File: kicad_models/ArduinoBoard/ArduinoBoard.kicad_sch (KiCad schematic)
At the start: 7 parts, among them J1 5V Output, J2 Buttons, J3 PWM Output, J4 Screw_Terminal_01x02, J5 Conn_01x04_Pin, J6 OLED

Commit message: Updated the KiCad files.
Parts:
- removed J6: OLED, symbol Connector:Screw_Terminal_01x04
- added J6: OLED, Connector_PinHeader_2.54mm:PinHeader_1x04_P2.54mm_Vertical, symbol Connector:Conn_01x04_Pin
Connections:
- net at A1.23 (A4): now also J6.4 (Pin_4)
- net at A1.24 (A5): now also J6.3 (Pin_3)
- net at A1.27 (+5V), J1.2 (Pin_2): now also J6.2 (Pin_2)
- net at A1.4 (GND), J1.1 (Pin_1): now also J6.1 (Pin_1)
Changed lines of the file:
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@@
 	)
 	(junction
-		(at 137.16 59.69)
+		(at 129.54 130.81)
 		(diameter 0)
 		(color 0 0 0 0)
 	)
+	(junction
+		(at 115.57 57.15)
+		(diameter 0)
+		(color 0 0 0 0)
+	)
 	(wire
 		(pts
@@
 	(wire
 		(pts
+			(xy 152.4 135.89) (xy 152.4 104.14)
+		)
+		(stroke
+			(width 0)
+			(type default)
+		)
+	)
+	(wire
+		(pts
 			(xy 134.62 130.81) (xy 134.62 119.38)
 		)
@@
 	(wire
 		(pts
+			(xy 129.54 130.81) (xy 129.54 135.89)
+		)
+		(stroke
+			(width 0)
+			(type default)
+		)
+	)
+	(wire
+		(pts
 			(xy 134.62 130.81) (xy 165.1 130.81)
 		)
@@
 	(wire
 		(pts
+			(xy 130.81 135.89) (xy 132.08 135.89)
+		)
+		(stroke
+			(width 0)
+			(type default)
+		)
+	)
+	(wire
+		(pts
+			(xy 134.62 133.35) (xy 149.86 133.35)
+		)
+		(stroke
+			(width 0)
+			(type default)
+		)
+	)
+	(wire
+		(pts
 			(xy 168.91 104.14) (xy 168.91 118.11)
 		)
@@
 	(wire
 		(pts
-			(xy 137.16 59.69) (xy 154.94 59.69)
+			(xy 137.16 135.89) (xy 152.4 135.89)
 		)
 		(stroke
@@
 	(wire
 		(pts
-			(xy 96.52 57.15) (xy 137.16 57.15)
+			(xy 96.52 57.15) (xy 115.57 57.15)
 		)
 		(stroke
@@
 	(wire
 		(pts
-			(xy 96.52 130.81) (xy 132.08 130.81)
+			(xy 96.52 130.81) (xy 129.54 130.81)
 		)
 		(stroke
@@
 	(wire
 		(pts
-			(xy 137.16 59.69) (xy 137.16 68.58)
+			(xy 144.78 104.14) (xy 152.4 104.14)
 		)
 		(stroke
@@
 	(wire
 		(pts
+			(xy 149.86 106.68) (xy 144.78 106.68)
+		)
+		(stroke
+			(width 0)
+			(type default)
+		)
+	)
+	(wire
+		(pts
 			(xy 170.18 120.65) (xy 165.1 120.65)
 		)
@@
 	(wire
 		(pts
+			(xy 129.54 130.81) (xy 132.08 130.81)
+		)
+		(stroke
+			(width 0)
+			(type default)
+		)
+	)
+	(wire
+		(pts
 			(xy 187.96 104.14) (xy 187.96 80.01)
 		)
@@
 	(wire
 		(pts
+			(xy 134.62 135.89) (xy 134.62 133.35)
+		)
+		(stroke
+			(width 0)
+			(type default)
+		)
+	)
+	(wire
+		(pts
 			(xy 184.15 100.33) (xy 184.15 82.55)
 		)
@@
 	(wire
 		(pts
+			(xy 130.81 125.73) (xy 130.81 135.89)
+		)
+		(stroke
+			(width 0)
+			(type default)
+		)
+	)
+	(wire
+		(pts
+			(xy 115.57 57.15) (xy 137.16 57.15)
+		)
+		(stroke
+			(width 0)
+			(type default)
+		)
+	)
+	(wire
+		(pts
+			(xy 115.57 125.73) (xy 130.81 125.73)
+		)
+		(stroke
+			(width 0)
+			(type default)
+		)
+	)
+	(wire
+		(pts
+			(xy 115.57 125.73) (xy 115.57 57.15)
+		)
+		(stroke
+			(width 0)
+			(type default)
+		)
+	)
+	(wire
+		(pts
 			(xy 96.52 72.39) (xy 96.52 130.81)
 		)
@@
 	(wire
 		(pts
-			(xy 137.16 57.15) (xy 137.16 59.69)
-		)
-		(stroke
-			(width 0)
-			(type default)
-		)
-	)
-	(wire
-		(pts
-			(xy 154.94 138.43) (xy 154.94 59.69)
+			(xy 137.16 57.15) (xy 137.16 68.58)
 		)
 		(stroke
@@
 		(pts
 			(xy 180.34 85.09) (xy 176.53 85.09)
+		)
+		(stroke
+			(width 0)
+			(type default)
+		)
+	)
+	(wire
+		(pts
+			(xy 149.86 133.35) (xy 149.86 106.68)
 		)
 		(stroke
@@
 	)
 	(symbol
-		(lib_id "Connector:Screw_Terminal_01x04")
-		(at 135.89 143.51 270)
+		(lib_id "Connector:Conn_01x04_Pin")
+		(at 132.08 140.97 90)
 		(unit 1)
 		(exclude_from_sim no)
@@
 		(fields_autoplaced yes)
 		(property "Reference" "J6"
-			(at 134.62 147.32 90)
+			(at 133.35 143.51 90)
 			(effects
 				(font
@@
 		)
 		(property "Value" "OLED"
-			(at 134.62 149.86 90)
-			(effects
-				(font
-					(size 1.27 1.27)
-				)
-			)
-		)
-		(property "Footprint" ""
-			(at 135.89 143.51 0)
+			(at 133.35 146.05 90)
+			(effects
+				(font
+					(size 1.27 1.27)
+				)
+			)
+		)
+		(property "Footprint" "Connector_PinHeader_2.54mm:PinHeader_1x04_P2.54mm_Vertical"
+			(at 132.08 140.97 0)
 			(effects
 				(font
@@
 		)
 		(property "Datasheet" "~"
-			(at 135.89 143.51 0)
-			(effects
-				(font
-					(size 1.27 1.27)
-				)
-				(hide yes)
-			)
-		)
-		(property "Description" "Generic screw terminal, single row, 01x04, script generated (kicad-library-utils/schlib/autogen/connector/)"
-			(at 135.89 143.51 0)
+			(at 132.08 140.97 0)
+			(effects
+				(font
+					(size 1.27 1.27)
+				)
+				(hide yes)
+			)
+		)
+		(property "Description" "Generic connector, single row, 01x04, script generated"
+			(at 132.08 140.97 0)
 			(effects
 				(font
@@
 		(pin "2"
 		)
+		(pin "4"
+		)
+		(pin "3"
+		)
 		(pin "1"
 		)
-		(pin "3"
-		)
-		(pin "4"
-		)
 		(instances
-			(project ""
+			(project "ArduinoBoard"
 				(path "/98bf385f-4cd5-4c0c-bda4-6735edf00281"
 					(reference "J6")

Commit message: Updated the PCB file I was working on.
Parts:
- added H1, H2, H3, H4: MountingHole, MountingHole:MountingHole_2.2mm_M2_DIN965_Pad, symbol Mechanical:MountingHole

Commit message: Updated the kicad files some more
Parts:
- J1, J2, J3, J4: footprint TerminalBlock:TerminalBlock_MaiXu_MX126-5.0-02P_1x02_P5.00mm -> TerminalBlock:TerminalBlock_bornier-2_P5.08mm
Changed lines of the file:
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@@
 			)
 		)
-		(property "Footprint" "TerminalBlock:TerminalBlock_MaiXu_MX126-5.0-02P_1x02_P5.00mm"
+		(property "Footprint" "TerminalBlock:TerminalBlock_bornier-2_P5.08mm"
 			(at 175.26 118.11 0)
 			(effects
@@
 			)
 		)
-		(property "Footprint" "TerminalBlock:TerminalBlock_MaiXu_MX126-5.0-02P_1x02_P5.00mm"
+		(property "Footprint" "TerminalBlock:TerminalBlock_bornier-2_P5.08mm"
 			(at 80.01 106.68 0)
 			(effects
@@
 			)
 		)
-		(property "Footprint" "TerminalBlock:TerminalBlock_MaiXu_MX126-5.0-02P_1x02_P5.00mm"
+		(property "Footprint" "TerminalBlock:TerminalBlock_bornier-2_P5.08mm"
 			(at 80.01 88.9 0)
 			(effects
@@
 			)
 		)
-		(property "Footprint" "TerminalBlock:TerminalBlock_MaiXu_MX126-5.0-02P_1x02_P5.00mm"
+		(property "Footprint" "TerminalBlock:TerminalBlock_bornier-2_P5.08mm"
 			(at 80.01 72.39 0)
 			(effects

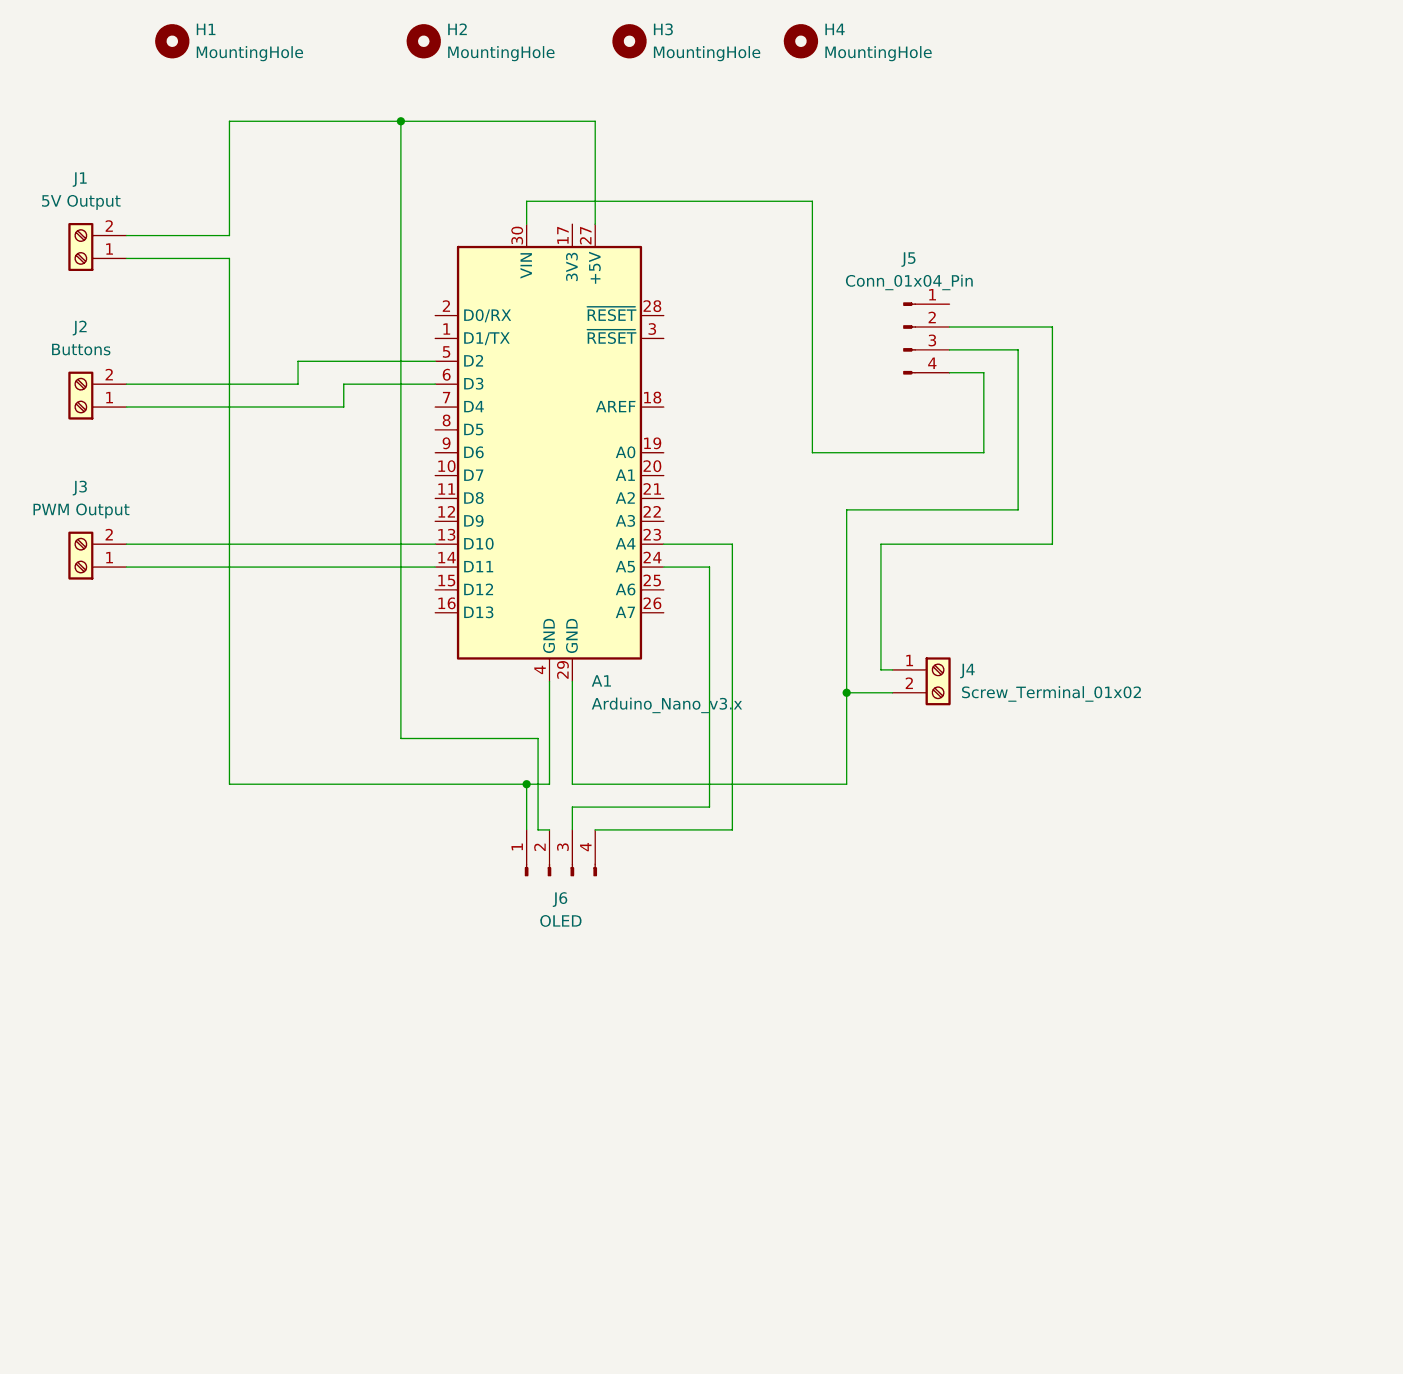
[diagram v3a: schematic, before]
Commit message: Had to make some updates after my first prototype PCB. Hopefully this version is correct. :)
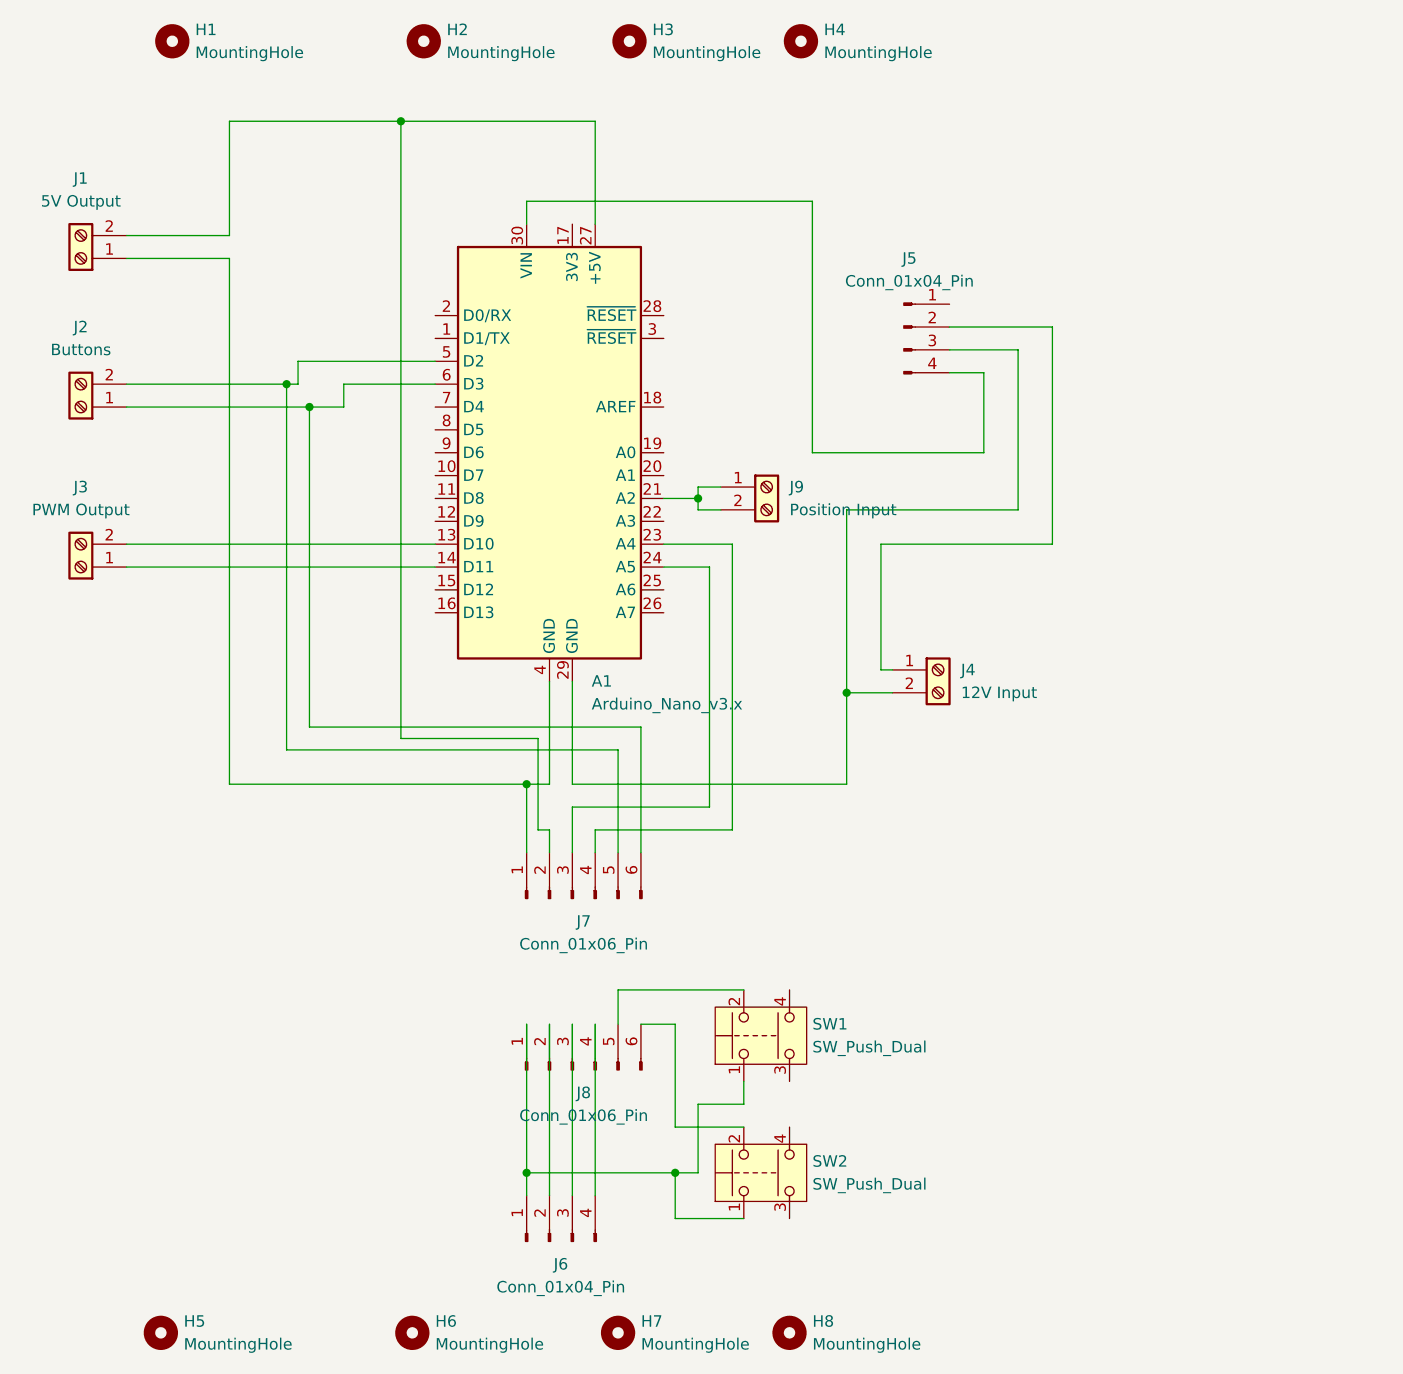
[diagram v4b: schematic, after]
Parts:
- added H5, H6, H7, H8: MountingHole, MountingHole:MountingHole_2.2mm_M2_DIN965_Pad, symbol Mechanical:MountingHole
- added J7, J8: Conn_01x06_Pin, Connector_PinHeader_2.54mm:PinHeader_1x06_P2.54mm_Vertical, symbol Connector:Conn_01x06_Pin
- added J9: Position Input, TerminalBlock:TerminalBlock_bornier-2_P5.08mm, symbol Connector:Screw_Terminal_01x02
- added SW1, SW2: SW_Push_Dual, Button_Switch_THT:SW_PUSH-12mm, symbol Switch:SW_Push_Dual
- J4: value Screw_Terminal_01x02 -> 12V Input
- J6: value OLED -> Conn_01x04_Pin
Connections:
- net at A1.21 (A2): now also J9.1 (Pin_1), J9.2 (Pin_2)
- net at A1.23 (A4): now also J7.4 (Pin_4); no longer J6.4 (Pin_4)
- net at A1.24 (A5): now also J7.3 (Pin_3); no longer J6.3 (Pin_3)
- net at A1.27 (+5V), J1.2 (Pin_2): now also J7.2 (Pin_2); no longer J6.2 (Pin_2)
- net at A1.4 (GND), J1.1 (Pin_1): now also J7.1 (Pin_1); no longer J6.1 (Pin_1)
- net at A1.5 (D2), J2.2 (Pin_2): now also J7.5 (Pin_5)
- net at A1.6 (D3), J2.1 (Pin_1): now also J7.6 (Pin_6)
- new net: J6.1 (Pin_1), J8.1 (Pin_1), SW1.1, SW2.1
- new net: J6.2 (Pin_2), J8.2 (Pin_2)
- new net: J6.3 (Pin_3), J8.3 (Pin_3)
- new net: J6.4 (Pin_4), J8.4 (Pin_4)
- new net: J8.6 (Pin_6), SW2.2
- new net: J8.5 (Pin_5), SW1.2

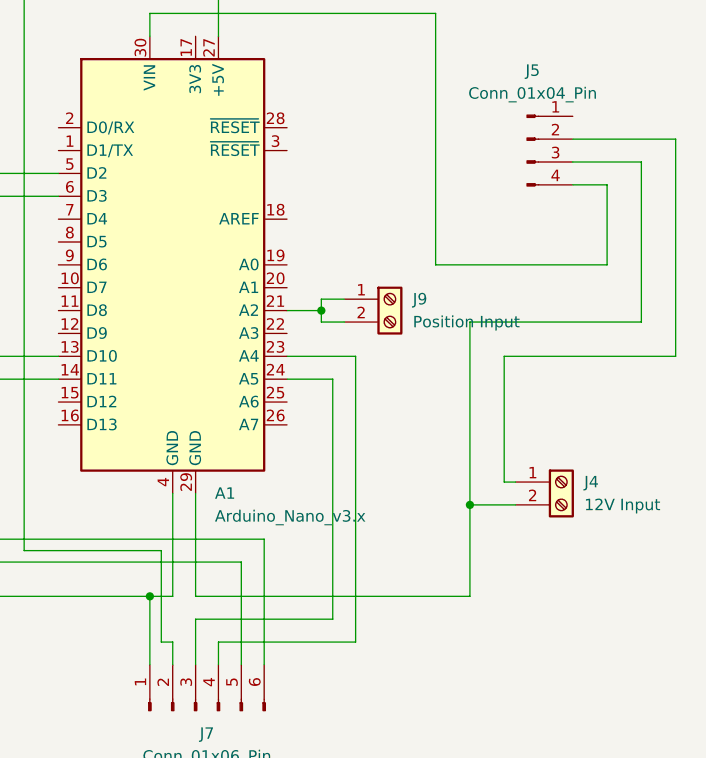
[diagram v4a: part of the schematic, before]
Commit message: Added a 0.1uF capacitor and linked the two GND pins on the Arduino. I seem to have overloaded the Arduino when I plugged in the 12V input - probably a surge. The capacitor should condition the circuit momentarily.
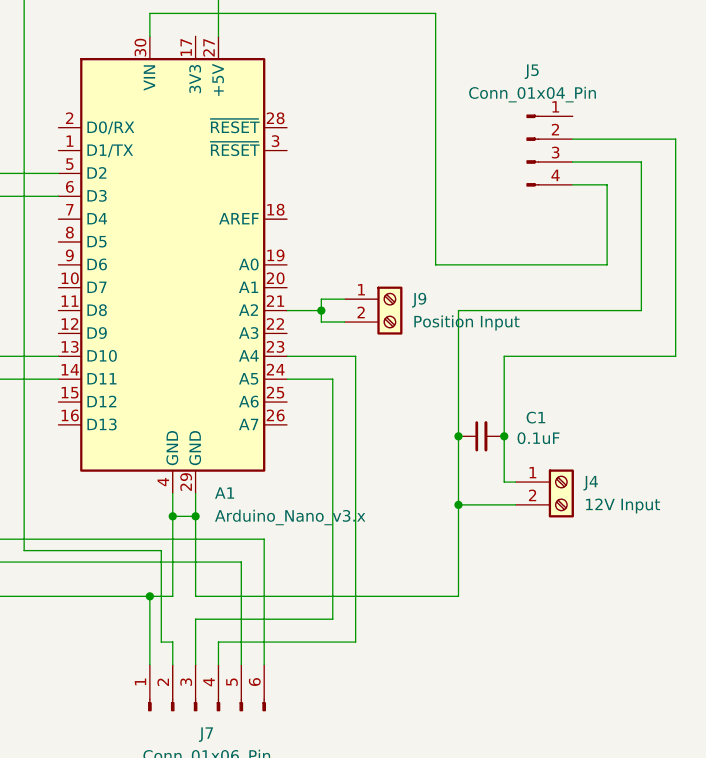
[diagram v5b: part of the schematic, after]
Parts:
- added C1: 0.1uF, Capacitor_THT:C_Disc_D3.0mm_W2.0mm_P2.50mm, symbol Device:C_Small
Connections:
- net at J4.1 (Pin_1), J5.2 (Pin_2): now also C1.2
- net at A1.29 (GND), J4.2 (Pin_2), J5.3 (Pin_3): now also A1.4 (GND), J1.1 (Pin_1), J7.1 (Pin_1), C1.1
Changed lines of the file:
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@@
 	(paper "A4")
 	(junction
-		(at 165.1 120.65)
+		(at 163.83 120.65)
 		(diameter 0)
 		(color 0 0 0 0)
@@
 	)
 	(junction
+		(at 134.62 121.92)
+		(diameter 0)
+		(color 0 0 0 0)
+	)
+	(junction
 		(at 115.57 57.15)
+		(diameter 0)
+		(color 0 0 0 0)
+	)
+	(junction
+		(at 163.83 113.03)
 		(diameter 0)
 		(color 0 0 0 0)
@@
 	)
 	(junction
+		(at 168.91 113.03)
+		(diameter 0)
+		(color 0 0 0 0)
+	)
+	(junction
+		(at 132.08 121.92)
+		(diameter 0)
+		(color 0 0 0 0)
+	)
+	(junction
 		(at 146.05 173.99)
 		(diameter 0)
@@
 	(wire
 		(pts
+			(xy 132.08 121.92) (xy 132.08 119.38)
+		)
+		(stroke
+			(width 0)
+			(type default)
+		)
+	)
+	(wire
+		(pts
 			(xy 180.34 93.98) (xy 180.34 85.09)
 		)
@@
 	(wire
 		(pts
-			(xy 134.62 130.81) (xy 134.62 119.38)
+			(xy 134.62 130.81) (xy 134.62 121.92)
 		)
 		(stroke
@@
 	(wire
 		(pts
-			(xy 165.1 100.33) (xy 184.15 100.33)
+			(xy 163.83 99.06) (xy 184.15 99.06)
 		)
 		(stroke
@@
 	(wire
 		(pts
-			(xy 132.08 130.81) (xy 132.08 119.38)
+			(xy 132.08 130.81) (xy 132.08 121.92)
 		)
 		(stroke
@@
 	(wire
 		(pts
-			(xy 134.62 130.81) (xy 165.1 130.81)
-		)
-		(stroke
-			(width 0)
-			(type default)
-		)
-	)
-	(wire
-		(pts
-			(xy 165.1 100.33) (xy 165.1 120.65)
+			(xy 134.62 130.81) (xy 163.83 130.81)
+		)
+		(stroke
+			(width 0)
+			(type default)
+		)
+	)
+	(wire
+		(pts
+			(xy 163.83 99.06) (xy 163.83 113.03)
 		)
 		(stroke
@@
 	(wire
 		(pts
-			(xy 168.91 104.14) (xy 168.91 118.11)
+			(xy 168.91 104.14) (xy 168.91 113.03)
 		)
 		(stroke
@@
 	(wire
 		(pts
-			(xy 165.1 120.65) (xy 165.1 130.81)
+			(xy 163.83 120.65) (xy 163.83 130.81)
 		)
 		(stroke
@@
 	(wire
 		(pts
-			(xy 170.18 120.65) (xy 165.1 120.65)
+			(xy 170.18 120.65) (xy 163.83 120.65)
 		)
 		(stroke
@@
 	(wire
 		(pts
+			(xy 168.91 113.03) (xy 168.91 118.11)
+		)
+		(stroke
+			(width 0)
+			(type default)
+		)
+	)
+	(wire
+		(pts
 			(xy 134.62 133.35) (xy 134.62 138.43)
 		)
@@
 	(wire
 		(pts
-			(xy 184.15 100.33) (xy 184.15 82.55)
+			(xy 184.15 99.06) (xy 184.15 82.55)
 		)
 		(stroke
@@
 	(wire
 		(pts
+			(xy 132.08 121.92) (xy 134.62 121.92)
+		)
+		(stroke
+			(width 0)
+			(type default)
+		)
+	)
+	(wire
+		(pts
 			(xy 102.87 86.36) (xy 104.14 86.36)
 		)
@@
 	(wire
 		(pts
+			(xy 134.62 121.92) (xy 134.62 119.38)
+		)
+		(stroke
+			(width 0)
+			(type default)
+		)
+	)
+	(wire
+		(pts
 			(xy 146.05 173.99) (xy 146.05 179.07)
+		)
+		(stroke
+			(width 0)
+			(type default)
+		)
+	)
+	(wire
+		(pts
+			(xy 163.83 113.03) (xy 163.83 120.65)
 		)
 		(stroke
@@
 					(unit 1)
 				)
+			)
+		)
+	)
+	(symbol
+		(lib_id "Device:C_Small")
+		(at 166.37 113.03 90)
+		(unit 1)
+		(exclude_from_sim no)
+		(in_bom yes)
+		(on_board yes)
+		(dnp no)
+		(property "Reference" "C1"
+			(at 172.466 110.998 90)
+			(effects
+				(font
+					(size 1.27 1.27)
+				)
+			)
+		)
+		(property "Value" "0.1uF"
+			(at 172.72 113.284 90)
+			(effects
+				(font
+					(size 1.27 1.27)
+				)
+			)
+		)
+		(property "Footprint" "Capacitor_THT:C_Disc_D3.0mm_W2.0mm_P2.50mm"
+			(at 166.37 113.03 0)
+			(effects
+				(font
+					(size 1.27 1.27)
+				)
+				(hide yes)
+			)
+		)
+		(property "Datasheet" "~"
+			(at 166.37 113.03 0)
+			(effects
+				(font
+					(size 1.27 1.27)
+				)
+				(hide yes)
+			)
+		)
+		(property "Description" "Unpolarized capacitor, small symbol"
+			(at 166.37 113.03 0)
+			(effects
+				(font
+					(size 1.27 1.27)
+				)
+				(hide yes)
+			)
+		)
+		(pin "2"
+		)
+		(pin "1"
+		)
+		(instances
+			(project ""
+				(path "/98bf385f-4cd5-4c0c-bda4-6735edf00281"
+					(reference "C1")
+					(unit 1)
+				)
